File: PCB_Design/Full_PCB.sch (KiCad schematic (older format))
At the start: 7 parts

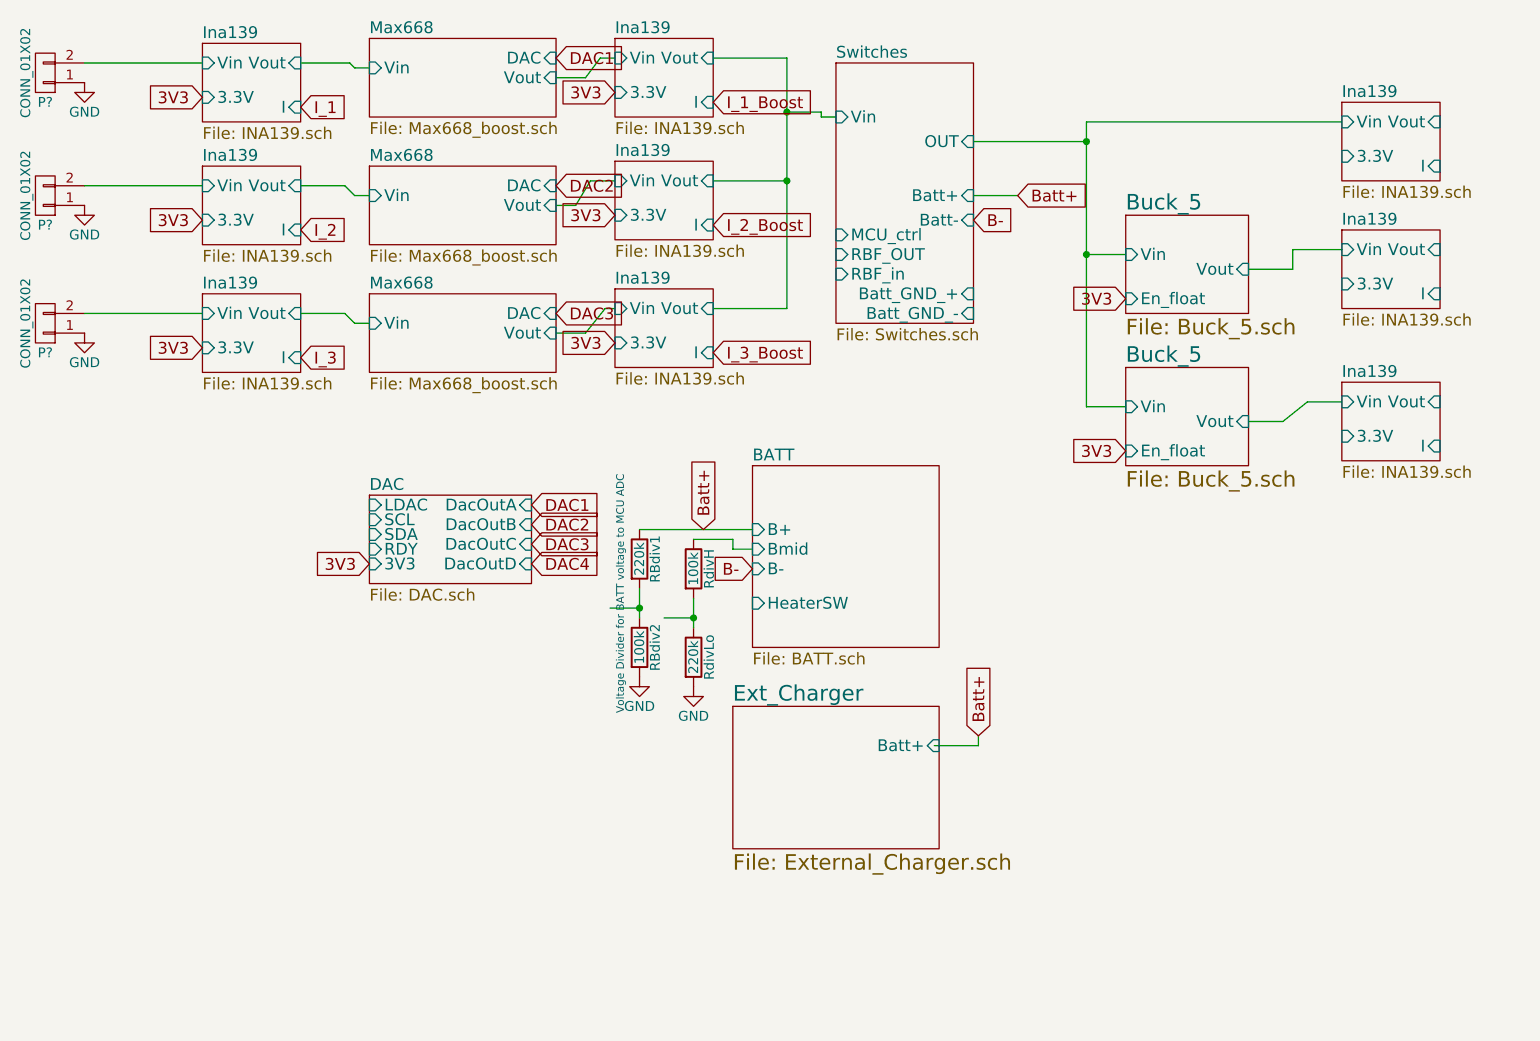
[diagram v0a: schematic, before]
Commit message: Updated PCB structure tree
Full_PCB now includes bottom and top layer hierarchical sheets
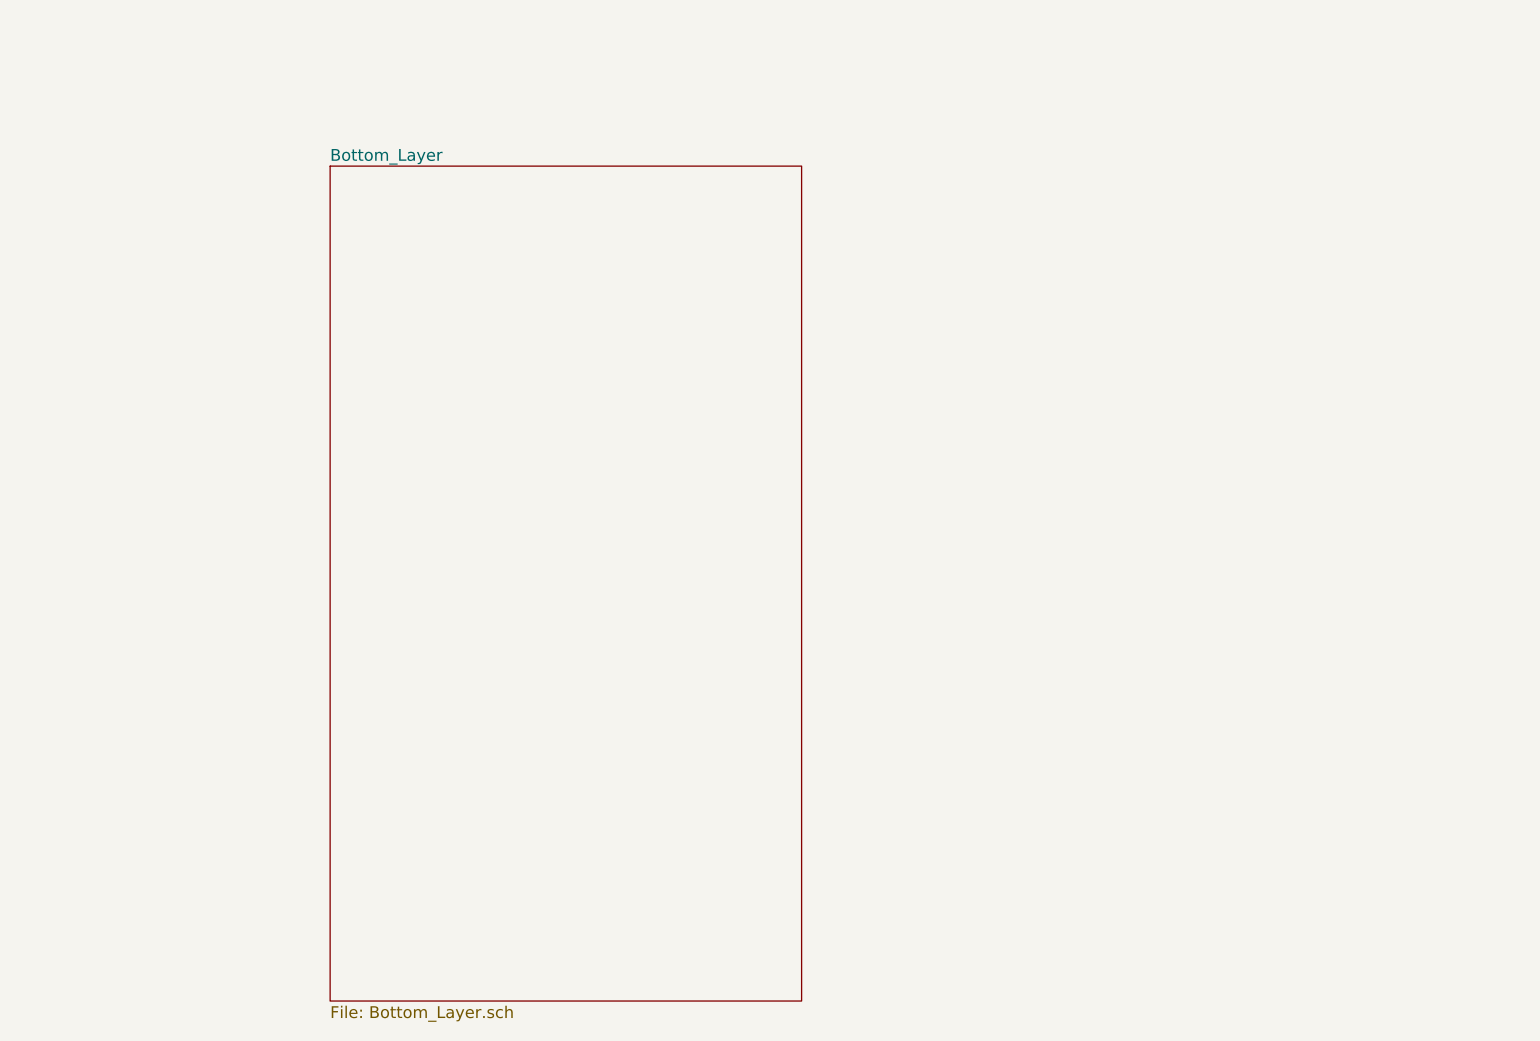
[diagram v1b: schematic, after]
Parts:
- removed P? (x3): CONN_01X02, symbol CONN_01X02
- removed RBdiv1, RdivLo: 220k, symbol R
- removed RBdiv2, RdivH: 100k, symbol R
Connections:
- net labels removed: 3V3, B-, Batt+, DAC1, DAC2, DAC3, DAC4, GND, I_1, I_1_Boost, I_2, I_2_Boost, I_3, I_3_Boost
- wire segments 50 -> 0
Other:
- note removed: "Voltage Divider for BATT voltage to MCU ADC"
